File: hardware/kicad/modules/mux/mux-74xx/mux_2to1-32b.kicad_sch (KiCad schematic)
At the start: 4 parts, among them U1 74LS157, U2 74LS157

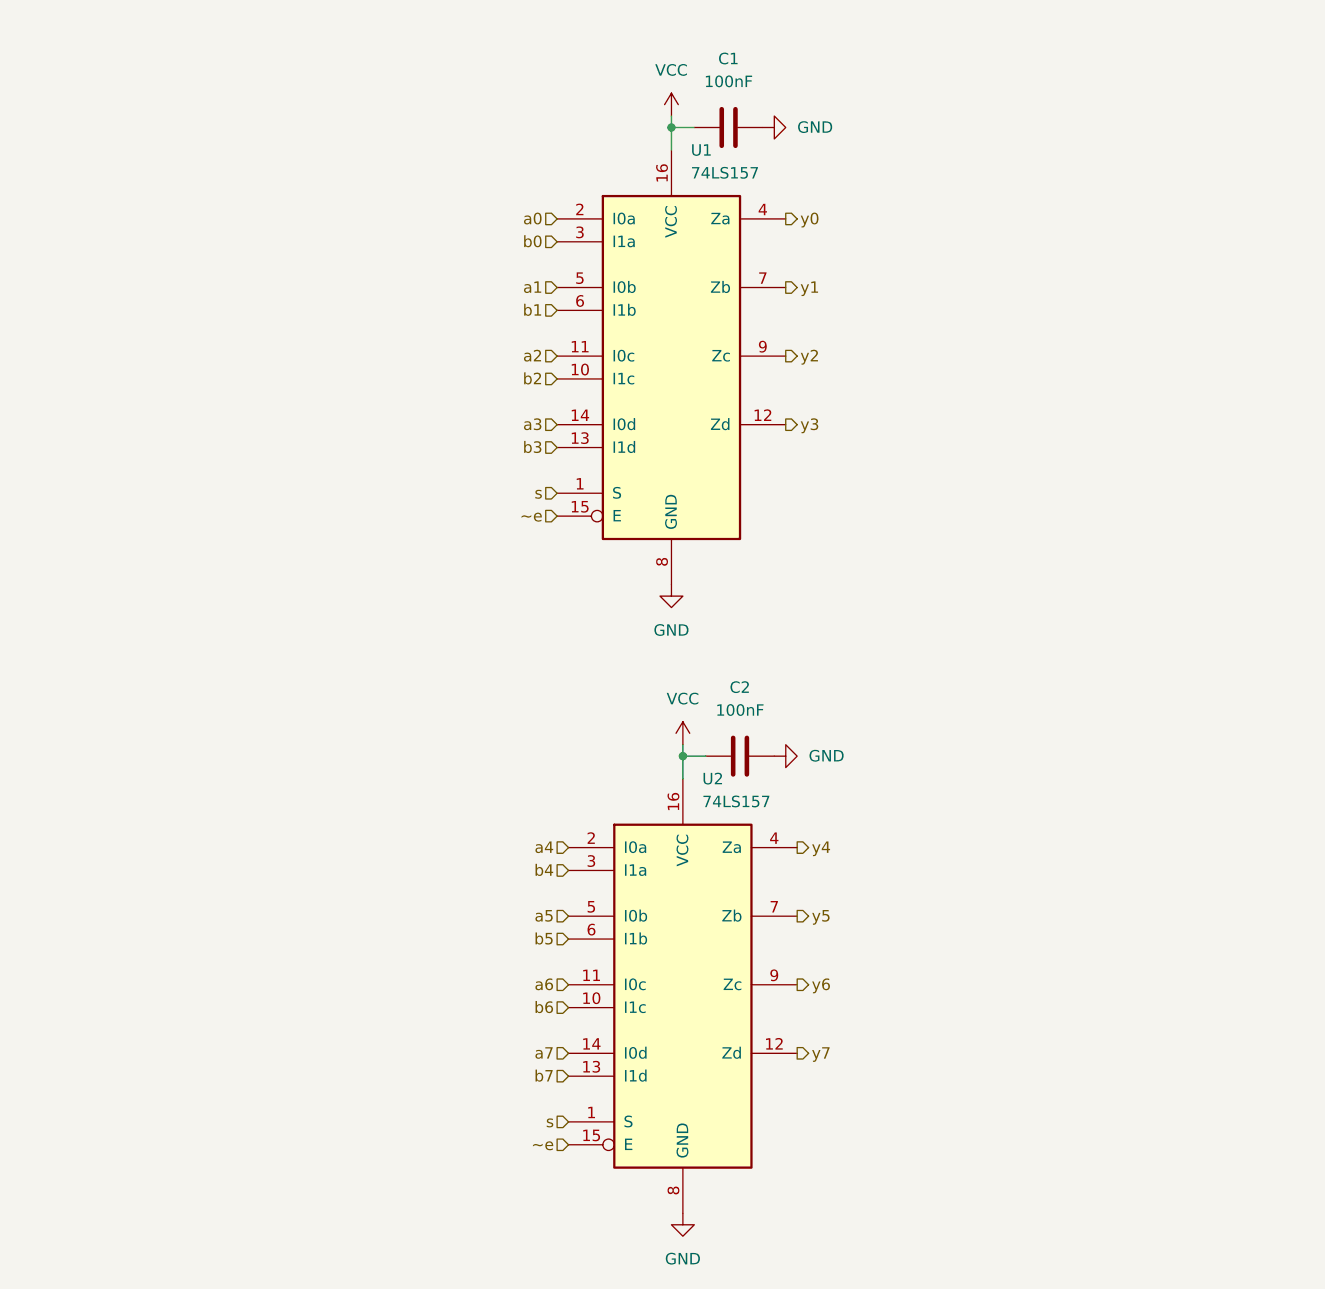
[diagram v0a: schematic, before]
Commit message: schematics: designed mux32_2to1
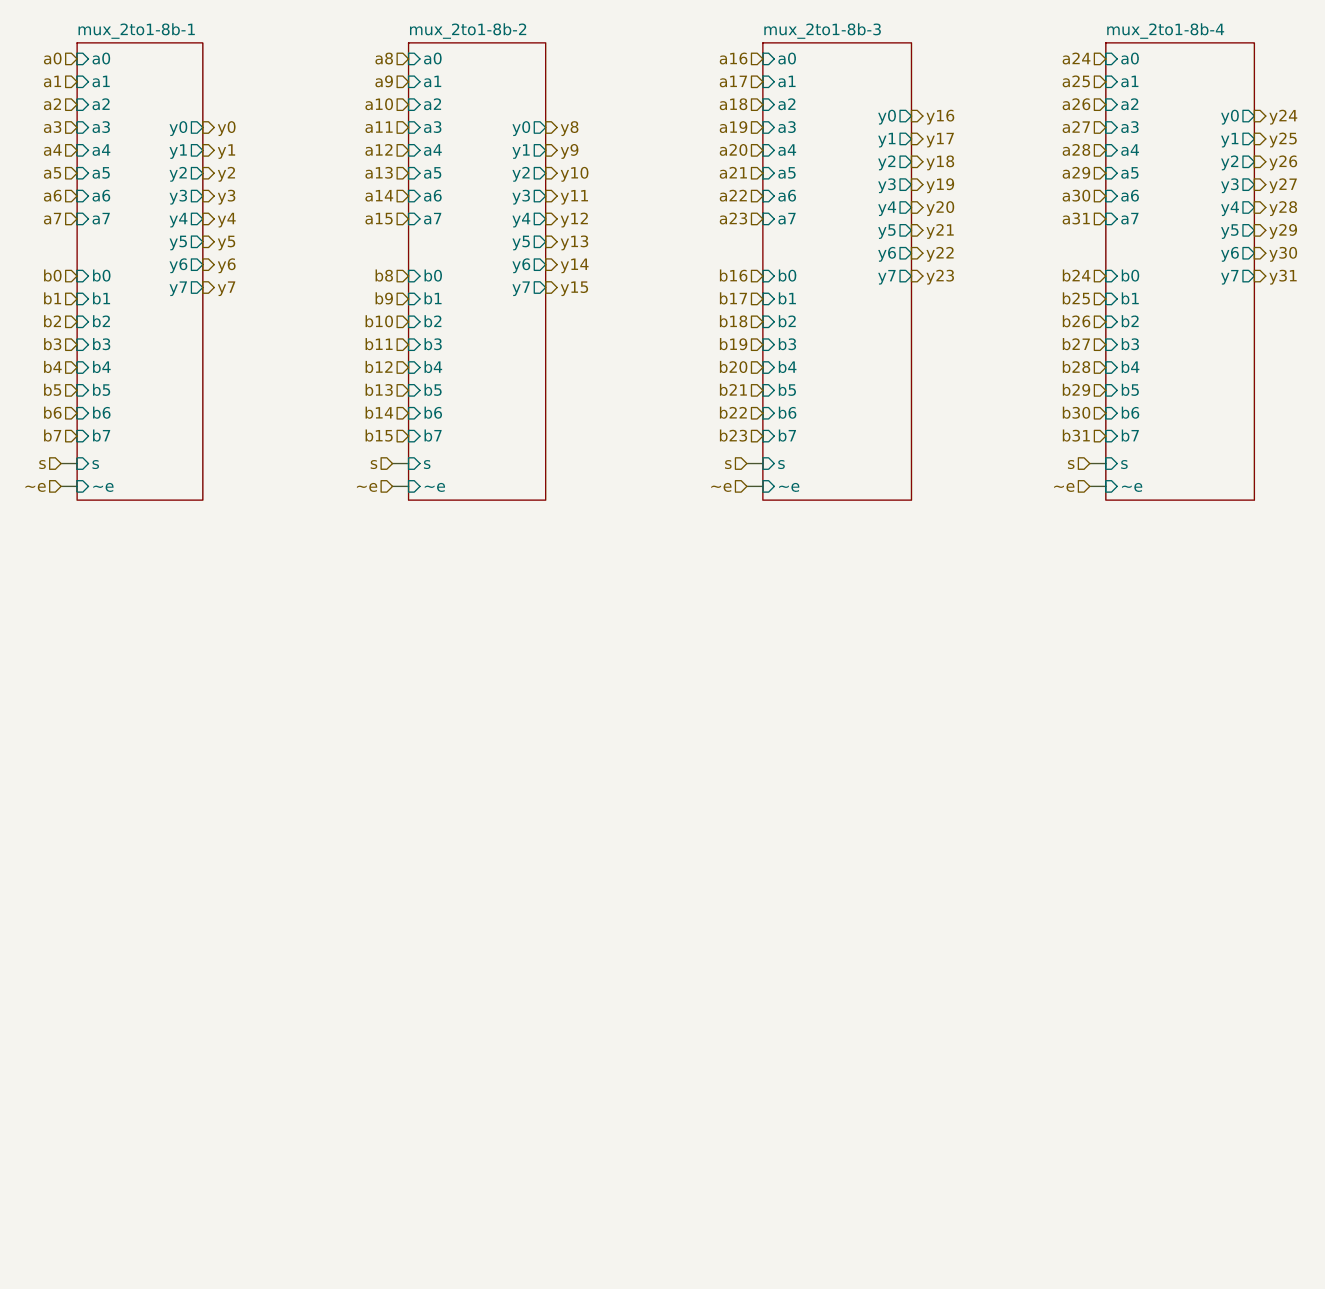
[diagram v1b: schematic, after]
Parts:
- removed C1, C2: 100nF, symbol Device:C
- removed U1, U2: 74LS157, symbol 74xx:74LS157
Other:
- added sheet mux_2to1-8b-1 (mux_2to1-8b.kicad_sch)
- added sheet mux_2to1-8b-2 (mux_2to1-8b.kicad_sch)
- added sheet mux_2to1-8b-3 (mux_2to1-8b.kicad_sch)
- added sheet mux_2to1-8b-4 (mux_2to1-8b.kicad_sch)
